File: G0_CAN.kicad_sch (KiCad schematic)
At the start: 0 parts

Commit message: Routed the G0B1 CAN board.
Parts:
- added C1, C5, C6: 100nF, Capacitor_SMD:C_0603_1608Metric, symbol Device:C
- added C10, C11: 10nF, Capacitor_SMD:C_0603_1608Metric, symbol Device:C
- added C7 (x2): 4700pF, Capacitor_SMD:C_0603_1608Metric, symbol Device:C
- added C8 (x2), C9 (x2): 47pF, Capacitor_SMD:C_0603_1608Metric, symbol Device:C
- added D1 (x2), D2 (x2): MMBZ27VC, Package_TO_SOT_SMD:SOT-23, symbol ESD:MMBZxxVC
- added D1: B5819W, Diode_SMD:D_SOD-123, symbol Device:D_Schottky
- added J1: USB_C_Receptacle_USB2.0, Connector_USB:USB_C_Receptacle_HRO_TYPE-C-31-M-12, symbol Connector:USB_C_Receptacle_USB2.0
- added J12: CAN1, Connector_JST:JST_EH_S3B-EH_1x03_P2.50mm_Horizontal, symbol Connector_Generic:Conn_01x03
- added J13: CAN2, Connector_JST:JST_EH_S3B-EH_1x03_P2.50mm_Horizontal, symbol Connector_Generic:Conn_01x03
- added R1 (x2), R2 (x2): 60.4, Resistor_SMD:R_0603_1608Metric, symbol Device:R
- added R1: 100k, Resistor_SMD:R_0603_1608Metric, symbol Device:R
- added R10 (x2): 22, Resistor_SMD:R_0603_1608Metric, symbol Device:R
- added R2, R3: 5.1k, Resistor_SMD:R_0603_1608Metric, symbol Device:R
- added U1: Nucleo-64-G0B1, Nucleo-64:Nucleo-64, symbol Nucleo-64:Nucleo-64-G0B1
- added U2, U3: TJA1051TK-3, Package_DFN_QFN:DFN-8-1EP_3x3mm_P0.65mm_EP1.55x2.4mm, symbol Interface_CAN_LIN:TJA1051TK-3
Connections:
- new net: C7.1, R1.2, R2.1 (x2)
- new net: J1.A5 (CC1), R3.2
- new net: C1.1, J1.S1 (SHIELD), R1.1
- new net: D1.2 (A), J1.A4 (VBUS), J1.A9 (VBUS), J1.B4 (VBUS), J1.B9 (VBUS)
- new net: J1.B5 (CC2), R2.2
- new net 3.3V: C10.2, C11.2, U1.16 (3.3v), U2.5 (VIO), U2.8 (S), U3.5 (VIO), U3.8 (S)
- new net 5V: C5.1, C6.1, U1.18 (5V), U2.3 (VCC), U3.3 (VCC)
- new net BTN: U1.23 (PC13)
- new net CAN1_H: C8.1, D1.1 (K), J12.1 (Pin_1), R1.1, U3.7 (CANH)
- new net CAN1_L: C9.2, D2.2 (K), J12.2 (Pin_2), R2.2, U3.6 (CANL)
- new net CAN1_RX: U1.73 (PC4), U3.4 (RXD)
- new net CAN1_TX: U1.75 (PC5), U3.1 (TXD)
- new net CAN2_H: C8.1, D1.1 (K), J13.1 (Pin_1), R1.1, U2.7 (CANH)
- new net CAN2_L: C9.2, D2.2 (K), J13.2 (Pin_2), R2.2, U2.6 (CANL)
- new net CAN2_RX: U1.35 (PC2), U2.4 (RXD)
- new net CAN2_TX: U1.37 (PC3), U2.1 (TXD)
- new net CLK: U1.29 (PF0)
- new net D+: J1.A6 (D+), J1.B6 (D+), R10.1
- new net D-: J1.A7 (D-), J1.B7 (D-), R10.1
- new net E5V: D1.1 (K), U1.6 (E5V)
- new net GND: C1.2, C10.1, C11.1, C5.2, C6.2, C7.2, C7.2, C8.2, C8.2, C9.1, C9.1, D1.2 (K), D1.2 (K), D2.1 (K), D2.1 (K), J1.A1 (GND), J1.A12 (GND), J1.B1 (GND), J1.B12 (GND), J12.3 (Pin_3), J13.3 (Pin_3), R1.2, R2.1, R3.1, U1.19 (GND), U1.20 (GND), U1.22 (GND), U1.47 (GND), U1.58 (GND), U1.70 (AGND), U1.8 (GND), U2.2 (GND), U2.9 (GND), U3.2 (GND), U3.9 (GND)
- new net LED: U1.49 (PA5)
- new net RCC_I: U1.25 (PC14)
- new net RCC_O: U1.27 (PC15)
- new net SDWIO: U1.13 (PA13)
- new net UART2_RX: U1.44 (PA3)
- new net UART2_TX: U1.72 (PA2)
- new net USB_DN: R10.2, U1.52 (PA11)
- new net USB_DP: R10.2, U1.50 (PA12)
- no-connect marks 0 -> 6

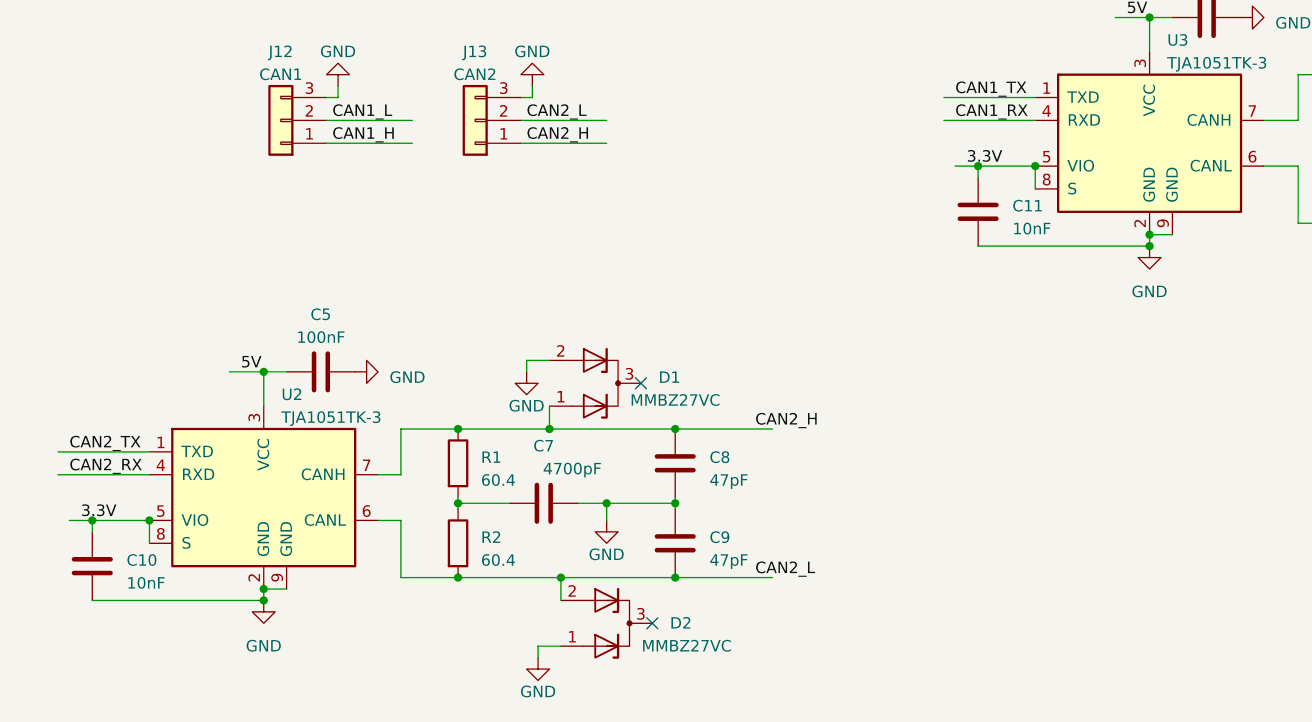
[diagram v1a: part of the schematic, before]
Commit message: Fix S pin on the CAN transcievers to low, so they are active. Fix USB data pin routing.
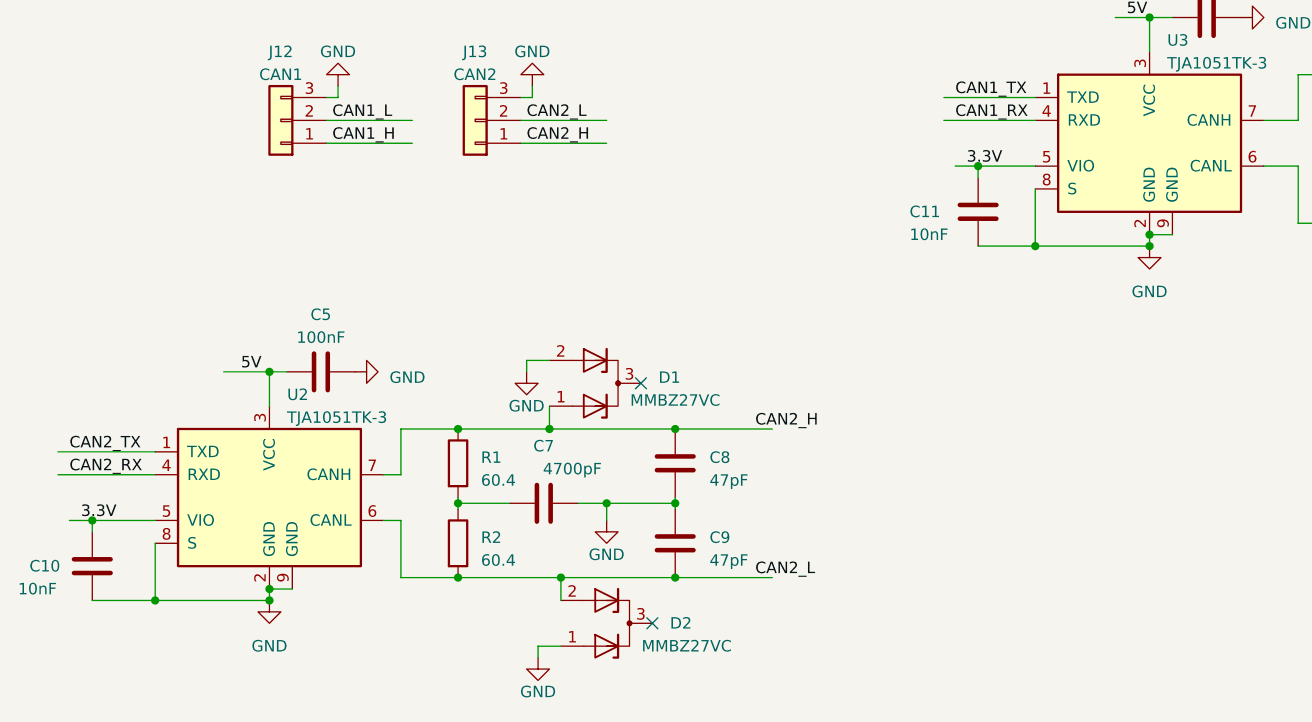
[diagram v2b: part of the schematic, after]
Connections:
- net 3.3V: no longer U2.8 (S), U3.8 (S)
- net GND: now also U2.8 (S), U3.8 (S)
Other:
- moved on the sheet: U2
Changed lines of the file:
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@@
   (junction (at 40.005 172.72) (diameter 0) (color 0 0 0 0)
   )
-  (junction (at 59.055 156.21) (diameter 0) (color 0 0 0 0)
-  )
   (junction (at 204.47 131.445) (diameter 0) (color 0 0 0 0)
   )
@@
   (junction (at 100.33 74.93) (diameter 0) (color 0 0 0 0)
   )
-  (junction (at 59.055 181.61) (diameter 0) (color 0 0 0 0)
-  )
   (junction (at 217.17 66.04) (diameter 0) (color 0 0 0 0)
   )
@@
   (junction (at 80.645 170.815) (diameter 0) (color 0 0 0 0)
   )
+  (junction (at 59.69 156.21) (diameter 0) (color 0 0 0 0)
+  )
   (junction (at 179.07 72.39) (diameter 0) (color 0 0 0 0)
   )
@@
   (junction (at 157.48 142.24) (diameter 0) (color 0 0 0 0)
   )
+  (junction (at 46.99 181.61) (diameter 0) (color 0 0 0 0)
+  )
   (junction (at 242.57 21.59) (diameter 0) (color 0 0 0 0)
   )
   (junction (at 104.14 74.93) (diameter 0) (color 0 0 0 0)
   )
+  (junction (at 144.78 142.24) (diameter 0) (color 0 0 0 0)
+  )
   (junction (at 180.34 131.445) (diameter 0) (color 0 0 0 0)
   )
   (junction (at 180.34 123.19) (diameter 0) (color 0 0 0 0)
   )
-  (junction (at 59.055 180.34) (diameter 0) (color 0 0 0 0)
-  )
   (junction (at 97.155 170.815) (diameter 0) (color 0 0 0 0)
   )
-  (junction (at 46.355 172.72) (diameter 0) (color 0 0 0 0)
+  (junction (at 59.69 180.34) (diameter 0) (color 0 0 0 0)
   )
   (junction (at 190.5 123.19) (diameter 0) (color 0 0 0 0)
   )
-  (junction (at 144.78 133.35) (diameter 0) (color 0 0 0 0)
+  (junction (at 59.69 181.61) (diameter 0) (color 0 0 0 0)
   )
   (junction (at 180.34 139.7) (diameter 0) (color 0 0 0 0)
@@
   (no_connect (at 102.235 184.15))
   (no_connect (at 201.93 144.78))
-  (wire (pts (xy 36.195 167.64) (xy 46.355 167.64))
+  (wire (pts (xy 36.195 167.64) (xy 46.99 167.64))
     (stroke (width 0) (type default))
   )
@@
     (stroke (width 0) (type default))
   )
-  (wire (pts (xy 59.055 180.34) (xy 59.055 181.61))
+  (wire (pts (xy 144.78 142.24) (xy 157.48 142.24))
     (stroke (width 0) (type default))
   )
@@
     (stroke (width 0) (type default))
   )
+  (wire (pts (xy 54.61 156.21) (xy 59.69 156.21))
+    (stroke (width 0) (type default))
+  )
   (wire (pts (xy 135.89 133.35) (xy 138.43 133.35))
     (stroke (width 0) (type default))
   )
-  (wire (pts (xy 59.055 156.21) (xy 59.055 160.02))
+  (wire (pts (xy 59.69 156.21) (xy 59.69 160.02))
     (stroke (width 0) (type default))
   )
@@
     (stroke (width 0) (type default))
   )
-  (wire (pts (xy 71.755 167.64) (xy 74.295 167.64))
+  (wire (pts (xy 72.39 167.64) (xy 74.295 167.64))
     (stroke (width 0) (type default))
   )
@@
     (stroke (width 0) (type default))
   )
-  (wire (pts (xy 36.195 165.1) (xy 46.355 165.1))
+  (wire (pts (xy 36.195 165.1) (xy 46.99 165.1))
     (stroke (width 0) (type default))
   )
@@
     (stroke (width 0) (type default))
   )
-  (wire (pts (xy 40.005 181.61) (xy 59.055 181.61))
+  (wire (pts (xy 40.005 181.61) (xy 46.99 181.61))
     (stroke (width 0) (type default))
   )
@@
     (stroke (width 0) (type default))
   )
-  (wire (pts (xy 46.355 172.72) (xy 46.355 175.26))
-    (stroke (width 0) (type default))
-  )
   (wire (pts (xy 57.15 77.47) (xy 62.23 77.47))
     (stroke (width 0) (type default))
@@
     (stroke (width 0) (type default))
   )
+  (wire (pts (xy 59.69 180.34) (xy 62.23 180.34))
+    (stroke (width 0) (type default))
+  )
   (wire (pts (xy 104.775 170.18) (xy 104.775 170.815))
     (stroke (width 0) (type default))
@@
     (stroke (width 0) (type default))
   )
-  (wire (pts (xy 61.595 156.21) (xy 59.055 156.21))
+  (wire (pts (xy 61.595 156.21) (xy 59.69 156.21))
     (stroke (width 0) (type default))
   )
@@
     (stroke (width 0) (type default))
   )
-  (wire (pts (xy 138.43 142.24) (xy 157.48 142.24))
+  (wire (pts (xy 138.43 142.24) (xy 144.78 142.24))
     (stroke (width 0) (type default))
   )
@@
     (stroke (width 0) (type default))
   )
+  (wire (pts (xy 144.78 135.89) (xy 144.78 142.24))
+    (stroke (width 0) (type default))
+  )
   (wire (pts (xy 157.48 140.97) (xy 157.48 142.24))
     (stroke (width 0) (type default))
@@
     (stroke (width 0) (type default))
   )
-  (wire (pts (xy 59.055 180.34) (xy 61.595 180.34))
-    (stroke (width 0) (type default))
-  )
-  (wire (pts (xy 40.005 172.72) (xy 46.355 172.72))
+  (wire (pts (xy 40.005 172.72) (xy 46.99 172.72))
     (stroke (width 0) (type default))
   )
@@
     (stroke (width 0) (type default))
   )
-  (wire (pts (xy 71.755 172.72) (xy 74.295 172.72))
+  (wire (pts (xy 72.39 172.72) (xy 74.295 172.72))
     (stroke (width 0) (type default))
   )
@@
     (stroke (width 0) (type default))
   )
+  (wire (pts (xy 46.99 181.61) (xy 59.69 181.61))
+    (stroke (width 0) (type default))
+  )
   (wire (pts (xy 100.33 54.61) (xy 106.68 54.61))
     (stroke (width 0) (type default))
@@
     (stroke (width 0) (type default))
   )
-  (wire (pts (xy 144.78 133.35) (xy 144.78 135.89))
-    (stroke (width 0) (type default))
-  )
   (wire (pts (xy 224.79 53.34) (xy 227.33 53.34))
     (stroke (width 0) (type default))
@@
     (stroke (width 0) (type default))
   )
+  (wire (pts (xy 59.69 180.34) (xy 59.69 181.61))
+    (stroke (width 0) (type default))
+  )
   (wire (pts (xy 187.96 147.32) (xy 187.96 148.59))
     (stroke (width 0) (type default))
@@
     (stroke (width 0) (type default))
   )
-  (wire (pts (xy 55.245 156.21) (xy 59.055 156.21))
+  (wire (pts (xy 46.99 175.26) (xy 46.99 181.61))
     (stroke (width 0) (type default))
   )
@@
     )
   )
-  (symbol (lib_id "power:GND") (at 59.055 181.61 0) (unit 1)
-    (in_bom yes) (on_board yes) (dnp no) (fields_autoplaced)
-    (property "Reference" "#PWR08" (at 59.055 187.96 0)
-      (effects (font (size 1.27 1.27)) hide)
-    )
-    (property "Value" "GND" (at 59.055 186.69 0)
-      (effects (font (size 1.27 1.27)))
-    )
-    (property "Footprint" "" (at 59.055 181.61 0)
-      (effects (font (size 1.27 1.27)) hide)
-    )
-    (property "Datasheet" "" (at 59.055 181.61 0)
+  (symbol (lib_id "power:GND") (at 59.69 181.61 0) (unit 1)
+    (in_bom yes) (on_board yes) (dnp no) (fields_autoplaced)
+    (property "Reference" "#PWR08" (at 59.69 187.96 0)
+      (effects (font (size 1.27 1.27)) hide)
+    )
+    (property "Value" "GND" (at 59.69 186.69 0)
+      (effects (font (size 1.27 1.27)))
+    )
+    (property "Footprint" "" (at 59.69 181.61 0)
+      (effects (font (size 1.27 1.27)) hide)
+    )
+    (property "Datasheet" "" (at 59.69 181.61 0)
       (effects (font (size 1.27 1.27)) hide)
     )
@@
   )
   (symbol (lib_id "Device:C") (at 40.005 177.8 180) (unit 1)
-    (in_bom yes) (on_board yes) (dnp no) (fields_autoplaced)
-    (property "Reference" "C10" (at 43.815 177.165 0)
+    (in_bom yes) (on_board yes) (dnp no)
+    (property "Reference" "C10" (at 33.02 177.8 0)
       (effects (font (size 1.27 1.27)) (justify right))
     )
-    (property "Value" "10nF" (at 43.815 179.705 0)
+    (property "Value" "10nF" (at 31.75 180.34 0)
       (effects (font (size 1.27 1.27)) (justify right))
     )
@@
     )
   )
-  (symbol (lib_id "Interface_CAN_LIN:TJA1051TK-3") (at 59.055 170.18 0) (unit 1)
-    (in_bom yes) (on_board yes) (dnp no) (fields_autoplaced)
-    (property "Reference" "U2" (at 61.0109 158.75 0)
+  (symbol (lib_id "Interface_CAN_LIN:TJA1051TK-3") (at 59.69 170.18 0) (unit 1)
+    (in_bom yes) (on_board yes) (dnp no) (fields_autoplaced)
+    (property "Reference" "U2" (at 61.6459 158.75 0)
       (effects (font (size 1.27 1.27)) (justify left))
     )
-    (property "Value" "TJA1051TK-3" (at 61.0109 161.29 0)
+    (property "Value" "TJA1051TK-3" (at 61.6459 161.29 0)
       (effects (font (size 1.27 1.27)) (justify left))
     )
-    (property "Footprint" "Package_DFN_QFN:DFN-8-1EP_3x3mm_P0.65mm_EP1.55x2.4mm" (at 59.055 182.88 0)
+    (property "Footprint" "Package_DFN_QFN:DFN-8-1EP_3x3mm_P0.65mm_EP1.55x2.4mm" (at 59.69 182.88 0)
       (effects (font (size 1.27 1.27) italic) hide)
     )
-    (property "Datasheet" "http://www.nxp.com/documents/data_sheet/TJA1051.pdf" (at 59.055 170.18 0)
-      (effects (font (size 1.27 1.27)) hide)
-    )
-    (property "LCSC Part #" "C1121846" (at 59.055 170.18 0)
-      (effects (font (size 1.27 1.27)) hide)
-    )
-    (property "Part #" "SIT1051TK/3" (at 59.055 170.18 0)
+    (property "Datasheet" "http://www.nxp.com/documents/data_sheet/TJA1051.pdf" (at 59.69 170.18 0)
+      (effects (font (size 1.27 1.27)) hide)
+    )
+    (property "LCSC Part #" "C1121846" (at 59.69 170.18 0)
+      (effects (font (size 1.27 1.27)) hide)
+    )
+    (property "Part #" "SIT1051TK/3" (at 59.69 170.18 0)
       (effects (font (size 1.27 1.27)) hide)
     )
@@
   )
   (symbol (lib_id "Device:C") (at 138.43 138.43 180) (unit 1)
-    (in_bom yes) (on_board yes) (dnp no) (fields_autoplaced)
-    (property "Reference" "C11" (at 142.24 137.795 0)
+    (in_bom yes) (on_board yes) (dnp no)
+    (property "Reference" "C11" (at 130.81 138.43 0)
       (effects (font (size 1.27 1.27)) (justify right))
     )
-    (property "Value" "10nF" (at 142.24 140.335 0)
+    (property "Value" "10nF" (at 130.81 140.97 0)
       (effects (font (size 1.27 1.27)) (justify right))
     )
